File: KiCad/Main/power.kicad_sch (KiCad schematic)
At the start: 50 parts, among them J10 Screw_Terminal_01x03, J11 Screw_Terminal_01x03, J12 Screw_Terminal_01x03, J13 Screw_Terminal_01x02, J14 Conn_01x03, J15 Screw_Terminal_01x03, J16 Screw_Terminal_01x02, J9 Screw_Terminal_01x03, SW1 SW_DPST, U10 L7805, U11 L7905, U8 CD74HC4051E, U9 TL074

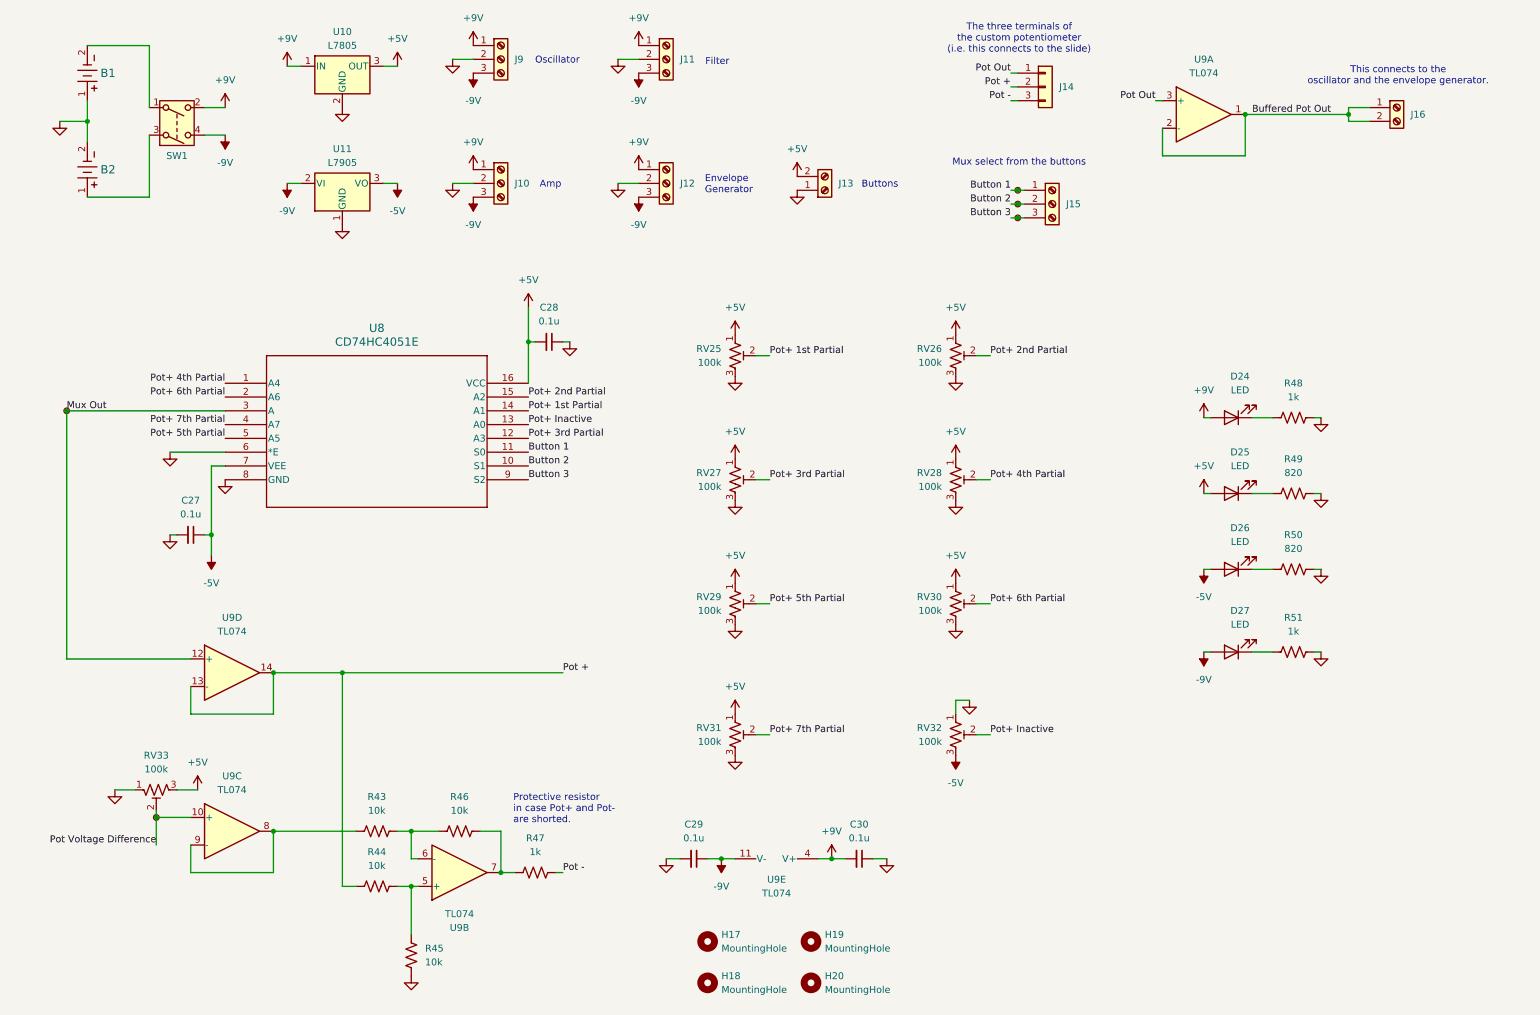
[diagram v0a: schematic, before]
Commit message: merged project into one combined board (excluding the buttons)
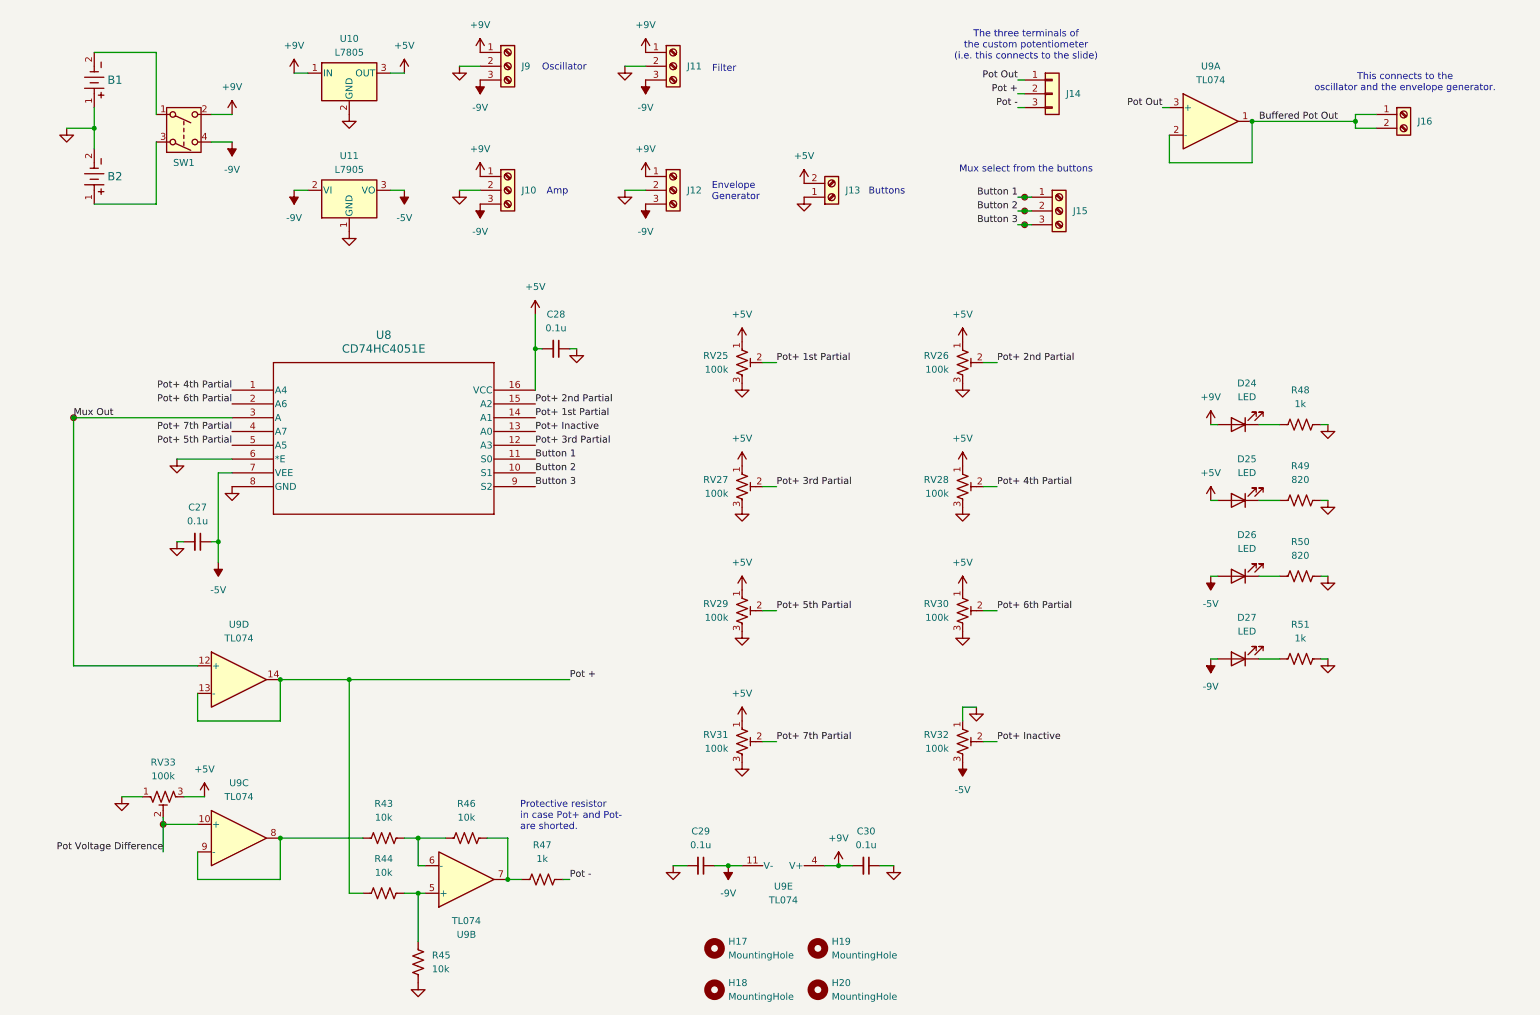
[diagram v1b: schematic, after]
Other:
- moved on the sheet: B1, B2, C27, C28, C29, C30, D24, D25, D26, D27, H17, H18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
